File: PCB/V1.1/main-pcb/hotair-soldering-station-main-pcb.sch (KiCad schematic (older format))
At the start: 62 parts, among them J1 230VAC_IN, J10 PB6, J11 PB4, J13 ICP (goldpin r2,54), J2 main-board-conn, J3 EARTH_GND, J4 24V_IN (NS-25 r2,54), J5 PSUPPLY (PWZ-02S r.3,96), J6 HOTAIR_FAN (JST r,2,54), J7 HOTAIR_MEAS (JST r.2,5)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

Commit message: UPDATE
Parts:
- removed J10: PB6, My-Footprints:WIRE_PAD_1,3mm, symbol Connector_Generic:Conn_01x01
- removed J11: PB4, My-Footprints:WIRE_PAD_1,3mm, symbol Connector_Generic:Conn_01x01
- added J?: SOLD_IRON (r.2,54), My-Footprints:Conn-01x06-N25-W6P, symbol Connector_Generic:Conn_01x06
- added R? (x2): 0R, Capacitors:0805, symbol Device:R
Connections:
- net labels added: MAX31855_HOTAIR_CS, MAX31855_IRON_CS, SPI1_MISO, SPI1_MOSI, SPI1_SCK
- wire segments 239 -> 251
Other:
- moved on the sheet: J9, R18, R?

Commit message: SCH V2.0
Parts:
- removed Q?: BC817, Package_TO_SOT_SMD:SOT-23, symbol Transistor_BJT:BC817
- removed U2, U?: LMV324, symbol Amplifier_Operational:LMV324
- added C?: 100n, Capacitors:0805, symbol Device:C
- added C? (x2): 10n, Capacitors:0805, symbol Device:C
- added GND_HEATER, GND_HEATER? (x2): GND2, XXX-00000, symbol SparkFun-PowerSymbols:GND2
- added Q?: BC807, Package_TO_SOT_SMD:SOT-23, symbol Transistor_BJT:BC807
- added Q? (x2): BC817, Package_TO_SOT_SMD:SOT-23, symbol Transistor_BJT:BC817
- added Q? (x2): FP3055LP, Package_TO_SOT_THT:TO-220-3_Vertical, symbol Device:Q_NMOS_GDS
- added R? (x4): 10k, Capacitors:0805, symbol Device:R
- added R? (x3): 30k, Capacitors:0805, symbol Device:R
- added R?: 0R, Capacitors:0805, symbol Device:R
- added R?: 4,7k, Capacitors:0805, symbol Device:R
- added R?: 100R, Capacitors:0805, symbol Device:R
- added R?: 1k, Capacitors:0805, symbol Device:R
- added U?: MAX31855KASA, Package_SO:SOIC-8_3.9x4.9mm_P1.27mm, symbol Sensor_Temperature:MAX31855KASA
- added U? (x3): LM358, Housings_SOIC:SO-8_5.3x6.2mm_Pitch1.27mm, symbol SparkFun-IC-Amplifiers:LM358
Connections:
- net labels added: HOTAIR_ADC, IRON_T12_ADC, IRON_T12_HEATER, IRON_T12_HEATER_CTRL, IRON_T12_THERM, IRON_WEP_HEATER, IRON_WEP_HEATER_CTRL, IRON_WEP_THERM, MAX31855_IRON_WEP_CS
- net labels removed: 7SEG_CLK, 7SEG_DIN, SOLDERING_IRON_HEATER_GND, SOLDERING_IRON_THERM, SOLD_IRON_HEATER_CTRL, THERM_HOTAIR_ADC, THERM_IRON_ADC
- wire segments 251 -> 307
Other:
- note added: "Heater control - T12"
- note added: "Heater control - WEP"
- moved on the sheet: C16, J9, J?, R18, R27, R?

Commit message: HV circuit resistor change, update footprints
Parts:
- removed F2, F3: Fuse, Fuse_Holders_and_Fuses:Fuseholder5x20_horiz_SemiClosed_Casing10x25mm, symbol Device:Fuse
- removed GND_HEATER, GND_HEATER? (x2): GND2, XXX-00000, symbol SparkFun-PowerSymbols:GND2
- removed R10, R15: 2x390R, Resistor_THT:R_Axial_DIN0414_L11.9mm_D4.5mm_P15.24mm_Horizontal, symbol Device:R
- removed R?: 0R, Capacitors:0805, symbol Device:R
- added C2: 100n, Capacitors:0805, symbol Device:C
- added F2: Polyfuse, Fuse:Fuse_Bourns_MF-RG500, symbol Device:Polyfuse
- added R13, R21, R8: 200R, Resistors_ThroughHole:R_Axial_DIN0207_L6.3mm_D2.5mm_P10.16mm_Horizontal, symbol Device:R
- added R23, R26: 50R, Resistors_ThroughHole:R_Axial_DIN0207_L6.3mm_D2.5mm_P10.16mm_Horizontal, symbol Device:R
- F1: value Fuse -> 3,15A
- R12: footprint Resistor_THT:R_Axial_DIN0414_L11.9mm_D4.5mm_P15.24mm_Horizontal -> Resistors_ThroughHole:R_Axial_DIN0207_L6.3mm_D2.5mm_P10.16mm_Horizontal
- R17: value 100R -> 200R; footprint Resistor_THT:R_Axial_DIN0414_L11.9mm_D4.5mm_P15.24mm_Horizontal -> Resistors_ThroughHole:R_Axial_DIN0207_L6.3mm_D2.5mm_P10.16mm_Horizontal
- gave numbers to parts that had none: 28
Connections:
- net labels added: GND2
- wire segments 307 -> 311
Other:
- moved on the sheet: C5, C7, J8, Q6, R12

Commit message: Main board routing, remove old 7seg from front panel schematic
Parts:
- removed Q4: FP3055LP, Package_TO_SOT_THT:TO-220-3_Vertical, symbol Device:Q_NMOS_GDS
- added Q4: Q_PMOS_GDS, Power_Integrations:TO-220, symbol Device:Q_PMOS_GDS
- C14, C15: footprint Capacitors_THT:CP_Radial_D10.0mm_P5.00mm -> Capacitors_ThroughHole:CP_Radial_D10.0mm_P5.00mm
- J10: footprint My-Footprints:Conn-01x06-N25-W6P -> My-Footprints:Conn_1x06
- U6: footprint Housings_SOIC:SO-8_5.3x6.2mm_Pitch1.27mm -> Package_SO:SO-8_3.9x4.9mm_P1.27mm
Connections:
- net labels added: GND_HEATER
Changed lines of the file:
@@
 F 0 "C14" H 11218 6921 50  0000 L CNN
 F 1 "330u/35V" H 11218 6830 50  0000 L CNN
-F 2 "Capacitors_THT:CP_Radial_D10.0mm_P5.00mm" H 11138 6725 50  0001 C CNN
+F 2 "Capacitors_ThroughHole:CP_Radial_D10.0mm_P5.00mm" H 11138 6725 50  0001 C CNN
 F 3 "~" H 11100 6875 50  0001 C CNN
 	1    11100 6875
@@
 F 0 "C15" H 11968 6921 50  0000 L CNN
 F 1 "330u/35V" H 11968 6830 50  0000 L CNN
-F 2 "Capacitors_THT:CP_Radial_D10.0mm_P5.00mm" H 11888 6725 50  0001 C CNN
+F 2 "Capacitors_ThroughHole:CP_Radial_D10.0mm_P5.00mm" H 11888 6725 50  0001 C CNN
 F 3 "~" H 11850 6875 50  0001 C CNN
 	1    11850 6875
@@
 Text GLabel 16450 9650 0    50   Input ~ 0
 HOTAIR_HEATER_CTRL
-Text GLabel 16450 9250 0    50   Input ~ 0
+Text GLabel 16450 9350 0    50   Input ~ 0
 IRON_WEP_HEATER_CTRL
 Wire Wire Line
@@
 F 0 "J10" H 11905 11792 50  0000 L CNN
 F 1 "SOLD_IRON (r.2,54)" H 11905 11701 50  0000 L CNN
-F 2 "My-Footprints:Conn-01x06-N25-W6P" H 11825 11800 50  0001 C CNN
+F 2 "My-Footprints:Conn_1x06" H 11825 11800 50  0001 C CNN
 F 3 "~" H 11825 11800 50  0001 C CNN
 	1    11825 11800
@@
 Text GLabel 11400 12100 0    50   Input ~ 0
 THERM_GND
-Text GLabel 16450 9550 0    50   Input ~ 0
+Text GLabel 18450 9650 2    50   Input ~ 0
 MAX31855_HOTAIR_CS
-Text GLabel 16450 9350 0    50   Input ~ 0
+Text GLabel 16450 9250 0    50   Input ~ 0
 MAX31855_IRON_CS
 $Comp
@@
 Wire Wire Line
 	3175 9200 3175 9125
-$Comp
-L Device:Q_NMOS_GDS Q4
-U 1 1 61023CA0
-P 3775 8650
-F 0 "Q4" H 3979 8696 50  0000 L CNN
-F 1 "FP3055LP" H 3979 8605 50  0000 L CNN
-F 2 "Package_TO_SOT_THT:TO-220-3_Vertical" H 3975 8750 50  0001 C CNN
-F 3 "~" H 3775 8650 50  0001 C CNN
-	1    3775 8650
-	1    0    0    1
-$EndComp
 Wire Wire Line
 	3875 8850 3875 9200
@@
 F 0 "U6" H 4875 12404 45  0000 C CNN
 F 1 "LM358" H 4875 12320 45  0000 C CNN
-F 2 "Housings_SOIC:SO-8_5.3x6.2mm_Pitch1.27mm" H 4875 12400 20  0001 C CNN
+F 2 "Package_SO:SO-8_3.9x4.9mm_P1.27mm" H 4875 12400 20  0001 C CNN
 F 3 "" H 4875 12050 50  0001 C CNN
 F 4 "IC-09172" H 4875 12331 60  0001 C CNN "Pole4"
@@
 F 0 "U6" H 11075 10429 45  0000 C CNN
 F 1 "LM358" H 11075 10345 45  0000 C CNN
-F 2 "Housings_SOIC:SO-8_5.3x6.2mm_Pitch1.27mm" H 11075 10425 20  0001 C CNN
+F 2 "Package_SO:SO-8_3.9x4.9mm_P1.27mm" H 11075 10425 20  0001 C CNN
 F 3 "" H 11075 10075 50  0001 C CNN
 F 4 "IC-09172" H 11075 10356 60  0001 C CNN "Pole4"
@@
 F 0 "U6" H 11928 8917 45  0000 L CNN
 F 1 "LM358" H 11928 8833 45  0000 L CNN
-F 2 "Housings_SOIC:SO-8_5.3x6.2mm_Pitch1.27mm" H 11800 9225 20  0001 C CNN
+F 2 "Package_SO:SO-8_3.9x4.9mm_P1.27mm" H 11800 9225 20  0001 C CNN
 F 3 "" H 11800 8875 50  0001 C CNN
 F 4 "IC-09172" H 11928 8791 60  0001 L CNN "Pole4"
@@
 Text GLabel 18450 8350 2    50   Input ~ 0
 SOLDER_DOWN_SW
-Text GLabel 18450 9650 2    50   Input ~ 0
+Text GLabel 16450 9550 0    50   Input ~ 0
 IRON_T12_HEATER_CTRL
 Wire Wire Line
@@
 Wire Notes Line
 	12700 4925 12700 14750
-$Comp
-L SparkFun-PowerSymbols:GND2 #GND_HEATER0101
-U 1 1 61549188
-P 11200 7800
-F 0 "#GND_HEATER0101" H 11250 7750 45  0001 L BNN
-F 1 "GND2" H 11308 7728 45  0000 L CNN
-F 2 "XXX-00000" H 11200 7475 60  0001 C CNN
-F 3 "" H 11200 7700 60  0001 C CNN
-	1    11200 7800
-	1    0    0    -1
-$EndComp
 Wire Wire Line
 	11425 7225 11425 7025
@@
 Wire Wire Line
 	2175 2475 2300 2475
+Text Label 11200 7700 0    50   ~ 0
+GND_HEATER
+$Comp
+L SparkFun-PowerSymbols:GND2 #GND_HEATER0101
+U 1 1 61549188
+P 11200 7800
+F 0 "#GND_HEATER0101" H 11250 7750 45  0001 L BNN
+F 1 "GND2" H 11308 7728 45  0000 L CNN
+F 2 "XXX-00000" H 11200 7475 60  0001 C CNN
+F 3 "" H 11200 7700 60  0001 C CNN
+	1    11200 7800
+	1    0    0    -1
+$EndComp
+$Comp
+L Device:Q_PMOS_GDS Q4
+U 1 1 611808C3
+P 3775 8650
+F 0 "Q4" H 3980 8696 50  0000 L CNN
+F 1 "Q_PMOS_GDS" H 3980 8605 50  0000 L CNN
+F 2 "Power_Integrations:TO-220" H 3975 8750 50  0001 C CNN
+F 3 "~" H 3775 8650 50  0001 C CNN
+	1    3775 8650
+	1    0    0    -1
+$EndComp
 $EndSCHEMATC

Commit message: uC change to STM32F103
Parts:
- added U8: STM32F103C6Tx, Package_QFP:LQFP-48_7x7mm_P0.5mm, symbol MCU_ST_STM32F1:STM32F103C6Tx
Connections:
- wire segments 311 -> 317
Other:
- moved on the sheet: U5
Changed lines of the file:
@@
 Text GLabel 18450 8950 2    50   Input ~ 0
 HOTAIR_UP_SW
-Text GLabel 16450 9150 0    50   Input ~ 0
+Text GLabel 16250 8550 0    50   Input ~ 0
 HOTAIR_DOWN_SW
 Text GLabel 18450 8850 2    50   Input ~ 0
@@
 L MCU_ST_STM32F0:STM32F030K6Tx U5
 U 1 1 5F834A58
-P 17450 8850
-F 0 "U5" H 17650 9800 50  0000 C CNN
-F 1 "STM32F030K6Tx" H 17900 9700 50  0000 C CNN
-F 2 "Package_QFP:LQFP-32_7x7mm_P0.8mm" H 16950 7950 50  0001 R CNN
-F 3 "http://www.st.com/st-web-ui/static/active/en/resource/technical/document/datasheet/DM00088500.pdf" H 17450 8850 50  0001 C CNN
-	1    17450 8850
+P 18925 10925
+F 0 "U5" H 19125 11875 50  0000 C CNN
+F 1 "STM32F030K6Tx" H 19375 11775 50  0000 C CNN
+F 2 "Package_QFP:LQFP-32_7x7mm_P0.8mm" H 18425 10025 50  0001 R CNN
+F 3 "http://www.st.com/st-web-ui/static/active/en/resource/technical/document/datasheet/DM00088500.pdf" H 18925 10925 50  0001 C CNN
+	1    18925 10925
 	1    0    0    -1
 $EndComp
@@
 L power:+3.3V #PWR0124
 U 1 1 5F836C06
-P 17450 7750
-F 0 "#PWR0124" H 17450 7600 50  0001 C CNN
-F 1 "+3.3V" H 17465 7923 50  0000 C CNN
-F 2 "" H 17450 7750 50  0001 C CNN
-F 3 "" H 17450 7750 50  0001 C CNN
-	1    17450 7750
-	1    0    0    -1
-$EndComp
-Wire Wire Line
-	17350 7950 17350 7900
-Wire Wire Line
-	17350 7900 17450 7900
-Wire Wire Line
-	17450 7900 17450 7950
-Wire Wire Line
-	17450 7900 17550 7900
-Wire Wire Line
-	17550 7900 17550 7950
-Connection ~ 17450 7900
-Wire Wire Line
-	17450 7750 17450 7900
+P 17350 6650
+F 0 "#PWR0124" H 17350 6500 50  0001 C CNN
+F 1 "+3.3V" H 17365 6823 50  0000 C CNN
+F 2 "" H 17350 6650 50  0001 C CNN
+F 3 "" H 17350 6650 50  0001 C CNN
+	1    17350 6650
+	1    0    0    -1
+$EndComp
+Wire Wire Line
+	17250 6850 17250 6800
+Wire Wire Line
+	17250 6800 17350 6800
+Wire Wire Line
+	17350 6800 17350 6850
+Wire Wire Line
+	17350 6800 17450 6800
+Wire Wire Line
+	17450 6800 17450 6850
+Connection ~ 17350 6800
+Wire Wire Line
+	17350 6650 17350 6800
 $Comp
 L power:GND #PWR0125
 U 1 1 5F85A980
-P 17400 10100
-F 0 "#PWR0125" H 17400 9850 50  0001 C CNN
-F 1 "GND" H 17405 9927 50  0000 C CNN
-F 2 "" H 17400 10100 50  0001 C CNN
-F 3 "" H 17400 10100 50  0001 C CNN
-	1    17400 10100
-	1    0    0    -1
-$EndComp
-Wire Wire Line
-	17350 9850 17350 9900
-Wire Wire Line
-	17350 9900 17400 9900
-Wire Wire Line
-	17450 9900 17450 9850
-Wire Wire Line
-	17400 10100 17400 9900
-Connection ~ 17400 9900
-Wire Wire Line
-	17400 9900 17450 9900
+P 17300 10100
+F 0 "#PWR0125" H 17300 9850 50  0001 C CNN
+F 1 "GND" H 17305 9927 50  0000 C CNN
+F 2 "" H 17300 10100 50  0001 C CNN
+F 3 "" H 17300 10100 50  0001 C CNN
+	1    17300 10100
+	1    0    0    -1
+$EndComp
+Wire Wire Line
+	17250 9850 17250 9900
+Wire Wire Line
+	17250 9900 17300 9900
+Wire Wire Line
+	17350 9900 17350 9850
+Wire Wire Line
+	17300 10100 17300 9900
+Connection ~ 17300 9900
+Wire Wire Line
+	17300 9900 17350 9900
 $Comp
 L Connector_Generic:Conn_01x06 J13
@@
 Wire Wire Line
 	18450 9450 17950 9450
-Text GLabel 16350 8150 0    50   Input ~ 0
+Text GLabel 16150 7050 0    50   Input ~ 0
 RST
 Wire Wire Line
-	16350 8150 16850 8150
+	16150 7050 16650 7050
 Wire Wire Line
 	18450 8850 17950 8850
@@
 	18450 8250 17950 8250
 Wire Wire Line
-	16850 9050 16450 9050
-Wire Wire Line
-	16450 9150 16850 9150
-Wire Wire Line
-	16850 9250 16450 9250
-Wire Wire Line
-	16450 9350 16850 9350
-Wire Wire Line
-	16450 9450 16850 9450
-Wire Wire Line
-	16850 9550 16450 9550
+	16650 8450 16250 8450
+Wire Wire Line
+	16250 8550 16650 8550
+Wire Wire Line
+	16650 8650 16250 8650
+Wire Wire Line
+	16250 8750 16650 8750
+Wire Wire Line
+	16250 8850 16650 8850
+Wire Wire Line
+	16650 8950 16250 8950
 Wire Wire Line
 	18450 8450 17950 8450
 Wire Wire Line
 	18450 8550 17950 8550
-Text GLabel 16425 8850 0    50   Input ~ 0
+Text GLabel 16225 8250 0    50   Input ~ 0
 HOTAIR_REED_SW
 Wire Wire Line
@@
 HOTAIR_FAN_UP_SW
 Wire Wire Line
-	16850 8750 16425 8750
-Wire Wire Line
-	16850 8850 16425 8850
+	16650 8150 16225 8150
+Wire Wire Line
+	16650 8250 16225 8250
 $Comp
 L Connector_Generic:Conn_01x06 J9
@@
 Wire Wire Line
 	19100 3000 19100 3425
-$Comp
-L power:GND #PWR0116
-U 1 1 5FA8FEE8
-P 16700 8475
-F 0 "#PWR0116" H 16700 8225 50  0001 C CNN
-F 1 "GND" H 16705 8302 50  0000 C CNN
-F 2 "" H 16700 8475 50  0001 C CNN
-F 3 "" H 16700 8475 50  0001 C CNN
-	1    16700 8475
-	1    0    0    -1
-$EndComp
-Wire Wire Line
-	16850 8350 16700 8350
-Wire Wire Line
-	16700 8350 16700 8475
 Wire Wire Line
 	11100 7025 11425 7025
@@
 Text GLabel 18450 8550 2    50   Input ~ 0
 BUZZER
-Text GLabel 16450 9650 0    50   Input ~ 0
+Text GLabel 16250 9050 0    50   Input ~ 0
 HOTAIR_HEATER_CTRL
-Text GLabel 16450 9350 0    50   Input ~ 0
+Text GLabel 16250 8750 0    50   Input ~ 0
 IRON_WEP_HEATER_CTRL
 Wire Wire Line
-	16450 9650 16850 9650
+	16250 9050 16650 9050
 Wire Wire Line
 	17950 9050 18450 9050
@@
 	1    0    0    -1
 $EndComp
-Text GLabel 16425 8750 0    50   Input ~ 0
+Text GLabel 16225 8150 0    50   Input ~ 0
 SOLDER_ON_SW
-Text GLabel 16450 9050 0    50   Input ~ 0
+Text GLabel 16250 8450 0    50   Input ~ 0
 SOLDER_UP_SW
 Text GLabel 18450 9350 2    50   Input ~ 0
 HOTAIR_ON_SW
-Text GLabel 16450 9450 0    50   Input ~ 0
+Text GLabel 16250 8850 0    50   Input ~ 0
 FAN_PWM
-Text Notes 15625 9975 0    50   ~ 0
+Text Notes 14275 9375 0    50   ~ 0
 TIM3_CH2 - PWM
-Text Notes 15625 10075 0    50   ~ 0
+Text Notes 14275 9475 0    50   ~ 0
 TIM14CH1 - Output compare (buzer)
 Text Notes 3925 2200 0    50   ~ 0
@@
 Text GLabel 18450 9650 2    50   Input ~ 0
 MAX31855_HOTAIR_CS
-Text GLabel 16450 9250 0    50   Input ~ 0
+Text GLabel 16250 8650 0    50   Input ~ 0
 MAX31855_IRON_CS
 $Comp
@@
 Text GLabel 18450 8350 2    50   Input ~ 0
 SOLDER_DOWN_SW
-Text GLabel 16450 9550 0    50   Input ~ 0
+Text GLabel 16250 8950 0    50   Input ~ 0
 IRON_T12_HEATER_CTRL
 Wire Wire Line
@@
 	11200 7700 11475 7700
 $Comp
-L SparkFun-PowerSymbols:GND2 #GND_HEATER0102
+L hotair-soldering-station-main-pcb-rescue:GND2-SparkFun-PowerSymbols #GND_HEATER0102
 U 1 1 615D2BEE
 P 11425 7225
@@
 $EndComp
 $Comp
-L SparkFun-PowerSymbols:GND2 #GND_HEATER0103
+L hotair-soldering-station-main-pcb-rescue:GND2-SparkFun-PowerSymbols #GND_HEATER0103
 U 1 1 615D2EB4
 P 10175 7075
@@
 	4125 10125 4125 10075
 $Comp
-L SparkFun-PowerSymbols:GND2 #GND_HEATER0104
+L hotair-soldering-station-main-pcb-rescue:GND2-SparkFun-PowerSymbols #GND_HEATER0104
 U 1 1 60E83A43
 P 10350 14350
@@
 GND_HEATER
 $Comp
-L SparkFun-PowerSymbols:GND2 #GND_HEATER0101
+L hotair-soldering-station-main-pcb-rescue:GND2-SparkFun-PowerSymbols #GND_HEATER0101
 U 1 1 61549188
 P 11200 7800
@@
 	1    0    0    -1
 $EndComp
+$Comp
+L MCU_ST_STM32F1:STM32F103C6Tx U8
+U 1 1 614AF30E
+P 17350 8350
+F 0 "U8" H 17725 9925 50  0000 C CNN
+F 1 "STM32F103C6Tx" H 17975 9850 50  0000 C CNN
+F 2 "Package_QFP:LQFP-48_7x7mm_P0.5mm" H 16750 6950 50  0001 R CNN
+F 3 "http://www.st.com/st-web-ui/static/active/en/resource/technical/document/datasheet/CD00210843.pdf" H 17350 8350 50  0001 C CNN
+	1    17350 8350
+	1    0    0    -1
+$EndComp
+Wire Wire Line
+	16500 7250 16500 7375
+Wire Wire Line
+	16650 7250 16500 7250
+$Comp
+L power:GND #PWR0116
+U 1 1 5FA8FEE8
+P 16500 7375
+F 0 "#PWR0116" H 16500 7125 50  0001 C CNN
+F 1 "GND" H 16505 7202 50  0000 C CNN
+F 2 "" H 16500 7375 50  0001 C CNN
+F 3 "" H 16500 7375 50  0001 C CNN
+	1    16500 7375
+	1    0    0    -1
+$EndComp
+Wire Wire Line
+	17250 9900 17150 9900
+Wire Wire Line
+	17150 9900 17150 9850
+Connection ~ 17250 9900
+Wire Wire Line
+	17350 9900 17450 9900
+Wire Wire Line
+	17450 9900 17450 9850
+Connection ~ 17350 9900
+Wire Wire Line
+	17450 6800 17550 6800
+Wire Wire Line
+	17550 6800 17550 6850
+Connection ~ 17450 6800
 $EndSCHEMATC

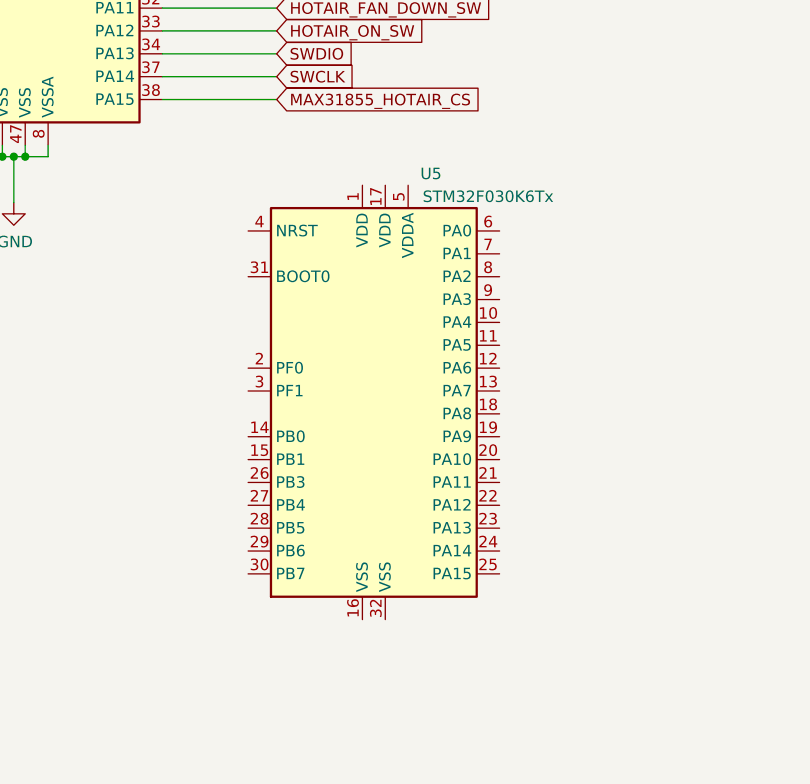
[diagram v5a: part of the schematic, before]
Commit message: Display change to LCD
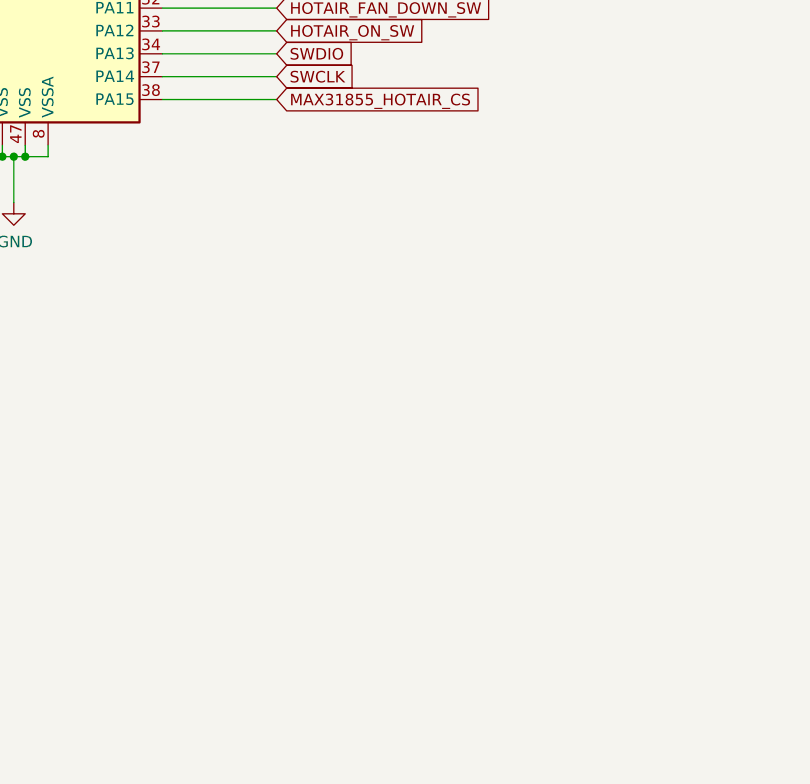
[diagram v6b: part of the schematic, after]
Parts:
- removed U5: STM32F030K6Tx, Package_QFP:LQFP-32_7x7mm_P0.8mm, symbol MCU_ST_STM32F0:STM32F030K6Tx
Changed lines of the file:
@@
 	650  12850 6525 12850
-$Comp
-L MCU_ST_STM32F0:STM32F030K6Tx U5
-U 1 1 5F834A58
-P 18925 10925
-F 0 "U5" H 19125 11875 50  0000 C CNN
-F 1 "STM32F030K6Tx" H 19375 11775 50  0000 C CNN
-F 2 "Package_QFP:LQFP-32_7x7mm_P0.8mm" H 18425 10025 50  0001 R CNN
-F 3 "http://www.st.com/st-web-ui/static/active/en/resource/technical/document/datasheet/DM00088500.pdf" H 18925 10925 50  0001 C CNN
-	1    18925 10925
-	1    0    0    -1
-$EndComp
 $Comp
 L power:+3.3V #PWR0124
